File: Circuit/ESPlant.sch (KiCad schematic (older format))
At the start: 13 parts

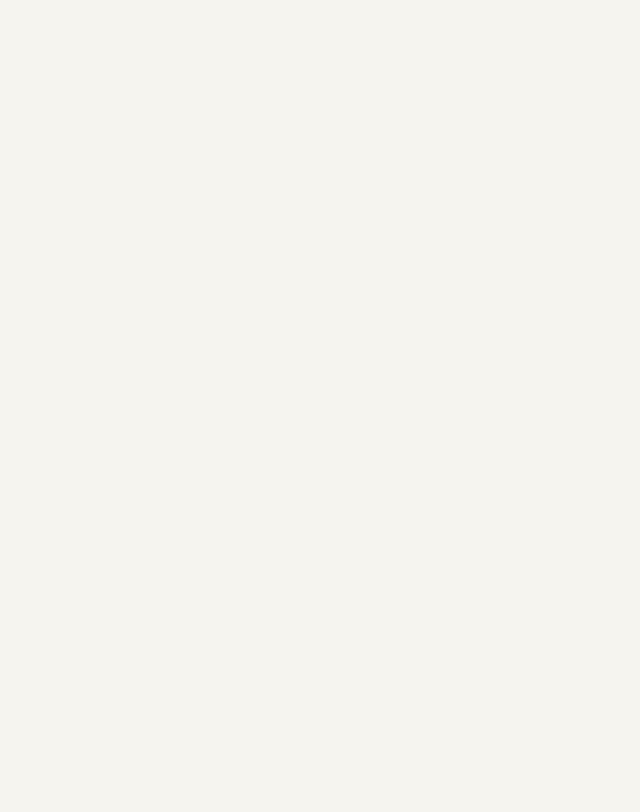
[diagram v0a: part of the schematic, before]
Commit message: Added UFQFPN48 footprint
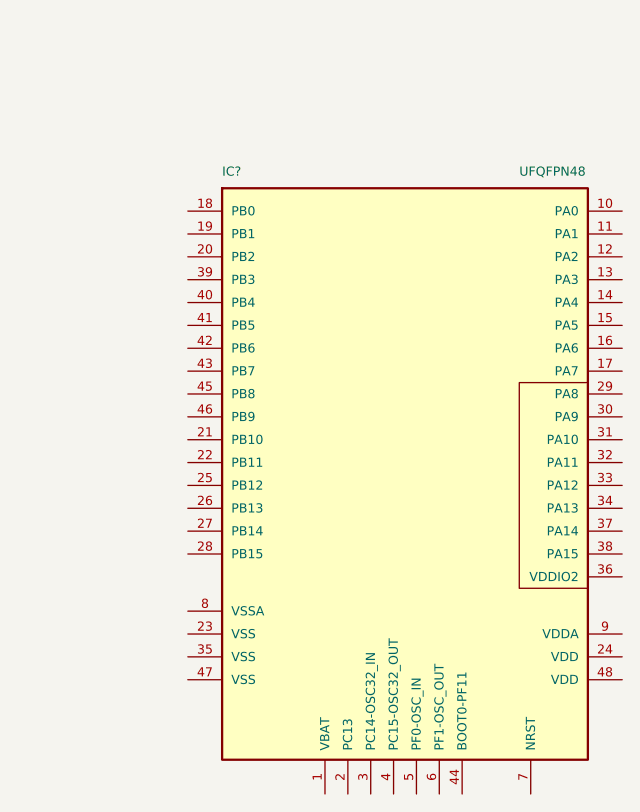
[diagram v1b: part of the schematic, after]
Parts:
- added IC?: UFQFPN48, symbol UFQFPN48
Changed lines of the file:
@@
 LIBS:valves
 LIBS:freetronics_schematic
-LIBS:basic_esp_board-cache
-LIBS:espkit-07-cache
 LIBS:ESPlant
 LIBS:ESPlant-cache
@@
 $EndComp
 NoConn ~ 3900 1700
+$Comp
+L UFQFPN48 IC?
+U 1 1 56379803
+P 5250 4000
+F 0 "IC?" H 4500 5250 40  0000 L BNN
+F 1 "UFQFPN48" H 5800 5250 40  0000 L BNN
+F 2 "" H 5250 4000 30  0000 C CIN
+F 3 "" H 5250 4000 60  0000 C CNN
+	1    5250 4000
+	1    0    0    -1
+$EndComp
 $EndSCHEMATC

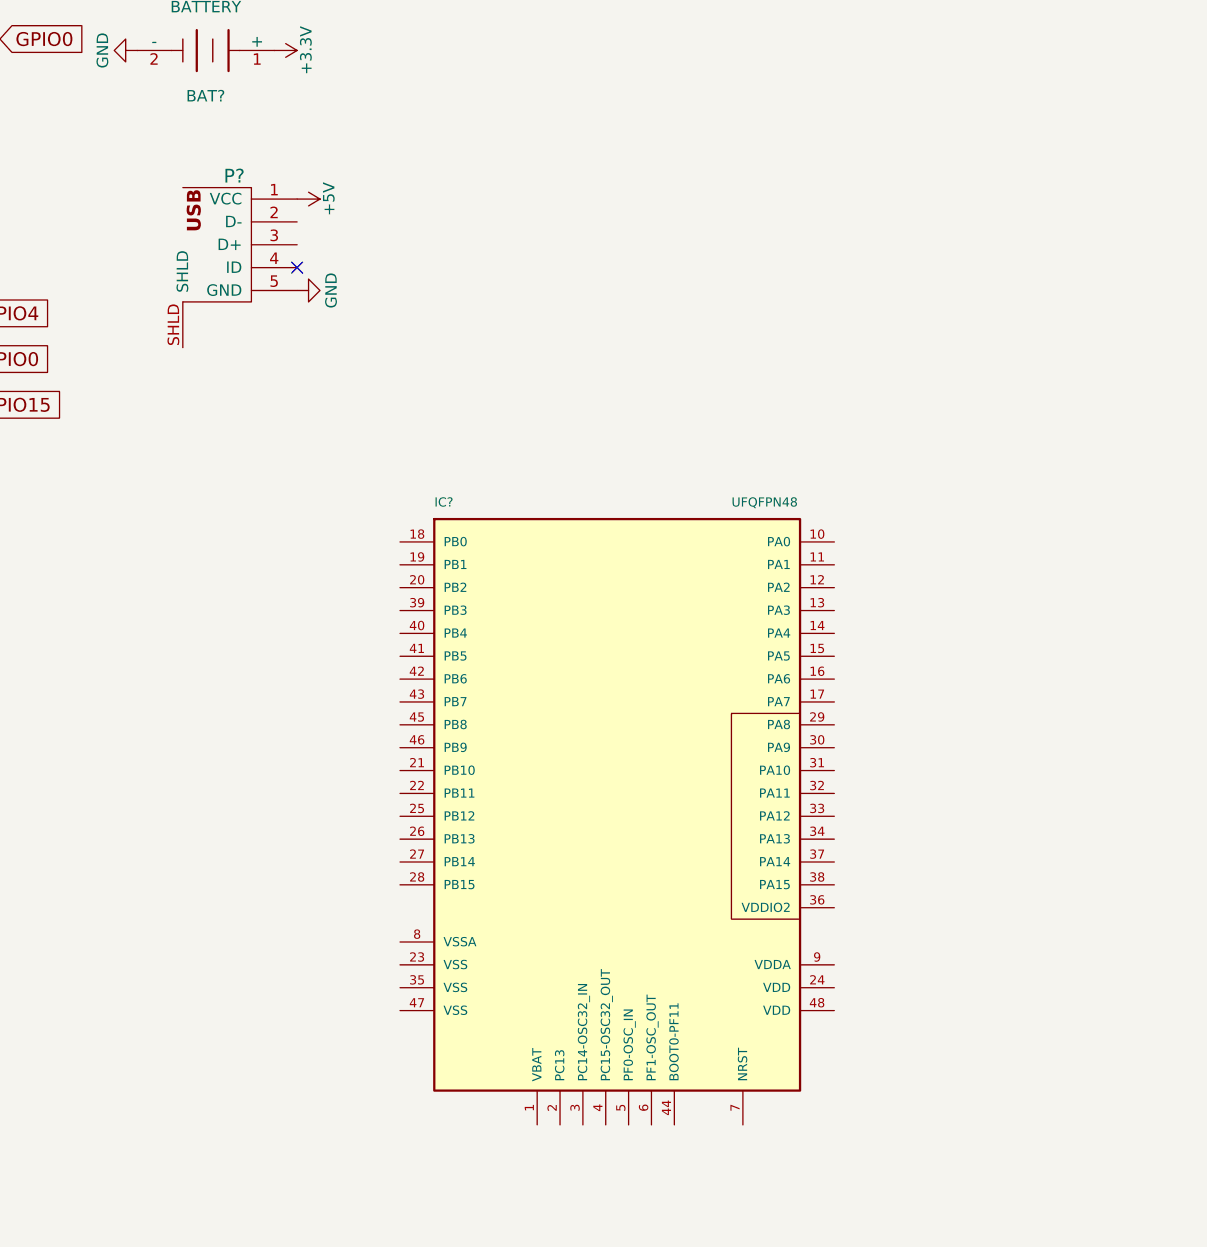
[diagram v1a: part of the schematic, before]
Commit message: Updated UFQFPN48 Footprint
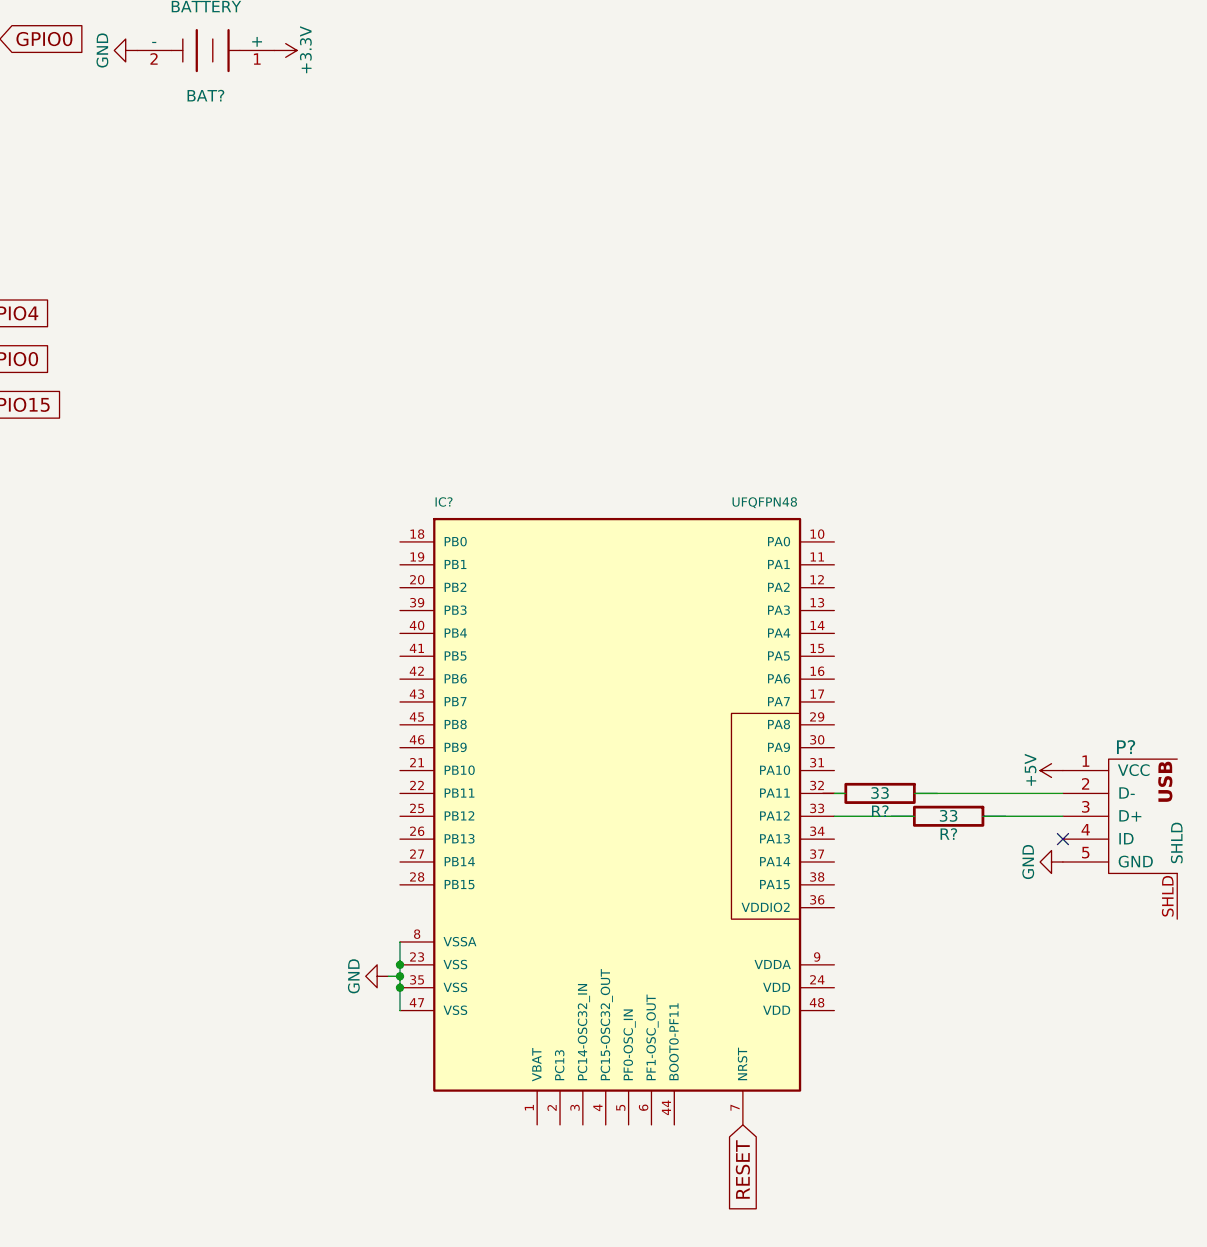
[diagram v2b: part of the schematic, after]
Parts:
- added R? (x2): 33, symbol R
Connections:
- wire segments 11 -> 17
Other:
- moved on the sheet: P?
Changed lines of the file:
@@
 L USB_5PIN_SHELL P?
 U 1 1 56377743
-P 3700 1550
-F 0 "P?" H 3625 1800 60  0000 C CNN
-F 1 "USB_5PIN_SHELL" H 3550 1200 60  0001 L CNN
-F 2 "FT:USB-MICRO_TH_4PEGS" H 3550 1150 31  0001 L CNN
-F 3 "" H 3700 1550 60  0000 C CNN
-	1    3700 1550
-	1    0    0    -1
+P 7450 4050
+F 0 "P?" H 7375 4300 60  0000 C CNN
+F 1 "USB_5PIN_SHELL" H 7300 3700 60  0001 L CNN
+F 2 "FT:USB-MICRO_TH_4PEGS" H 7300 3650 31  0001 L CNN
+F 3 "" H 7450 4050 60  0000 C CNN
+	1    7450 4050
+	-1   0    0    -1
 $EndComp
 $Comp
 L GND #PWR?
 U 1 1 56377AB6
-P 3900 1800
-F 0 "#PWR?" H 3900 1550 50  0001 C CNN
-F 1 "GND" H 3900 1650 50  0000 C CNN
-F 2 "" H 3900 1800 60  0000 C CNN
-F 3 "" H 3900 1800 60  0000 C CNN
-	1    3900 1800
-	0    -1   -1   0
+P 7250 4300
+F 0 "#PWR?" H 7250 4050 50  0001 C CNN
+F 1 "GND" H 7250 4150 50  0000 C CNN
+F 2 "" H 7250 4300 60  0000 C CNN
+F 3 "" H 7250 4300 60  0000 C CNN
+	1    7250 4300
+	0    1    -1   0
 $EndComp
 $Comp
@@
 L +5V #PWR?
 U 1 1 56378962
-P 3900 1400
-F 0 "#PWR?" H 3900 1250 50  0001 C CNN
-F 1 "+5V" H 3900 1540 50  0000 C CNN
-F 2 "" H 3900 1400 60  0000 C CNN
-F 3 "" H 3900 1400 60  0000 C CNN
-	1    3900 1400
-	0    1    1    0
+P 7250 3900
+F 0 "#PWR?" H 7250 3750 50  0001 C CNN
+F 1 "+5V" H 7250 4040 50  0000 C CNN
+F 2 "" H 7250 3900 60  0000 C CNN
+F 3 "" H 7250 3900 60  0000 C CNN
+	1    7250 3900
+	0    -1   1    0
 $EndComp
-NoConn ~ 3900 1700
+NoConn ~ 7250 4200
 $Comp
 L UFQFPN48 IC?
@@
 	1    0    0    -1
 $EndComp
+Text GLabel 5850 5450 3    60   Input ~ 0
+RESET
+$Comp
+L GND #PWR?
+U 1 1 56379DB5
+P 4300 4800
+F 0 "#PWR?" H 4300 4550 50  0001 C CNN
+F 1 "GND" H 4300 4650 50  0000 C CNN
+F 2 "" H 4300 4800 60  0000 C CNN
+F 3 "" H 4300 4800 60  0000 C CNN
+	1    4300 4800
+	0    1    1    0
+$EndComp
+Wire Wire Line
+	4350 4650 4350 4950
+Connection ~ 4350 4750
+Connection ~ 4350 4850
+Wire Wire Line
+	4300 4800 4350 4800
+Connection ~ 4350 4800
+$Comp
+L R R?
+U 1 1 5637A47F
+P 6450 4000
+F 0 "R?" V 6530 4000 50  0000 C CNN
+F 1 "33" V 6450 4000 50  0000 C CNN
+F 2 "" V 6380 4000 30  0000 C CNN
+F 3 "" H 6450 4000 30  0000 C CNN
+	1    6450 4000
+	0    1    1    0
+$EndComp
+$Comp
+L R R?
+U 1 1 5637A511
+P 6750 4100
+F 0 "R?" V 6830 4100 50  0000 C CNN
+F 1 "33" V 6750 4100 50  0000 C CNN
+F 2 "" V 6680 4100 30  0000 C CNN
+F 3 "" H 6750 4100 30  0000 C CNN
+	1    6750 4100
+	0    1    1    0
+$EndComp
+Wire Wire Line
+	7250 4000 6600 4000
+Wire Wire Line
+	6300 4000 6250 4000
+Wire Wire Line
+	6250 4100 6600 4100
+Wire Wire Line
+	6900 4100 7250 4100
 $EndSCHEMATC

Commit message: Updated Lithium power circuit
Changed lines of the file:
@@
 EESchema Schematic File Version 2
+LIBS:freetronics_schematic
 LIBS:power
 LIBS:device
@@
 LIBS:contrib
 LIBS:valves
-LIBS:freetronics_schematic
 LIBS:ESPlant
 LIBS:ESPlant-cache
@@
 $Descr A4 11693 8268
 encoding utf-8
-Sheet 1 1
+Sheet 1 2
 Title ""
 Date ""
@@
 Wire Wire Line
 	6900 4100 7250 4100
+$Sheet
+S 7500 950  2850 1900
+U 563C492E
+F0 "Power" 60
+F1 "Power.sch" 60
+$EndSheet
 $EndSCHEMATC

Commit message: Updated to use esp12e
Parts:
- removed BAT?: BATTERY, symbol BATTERY
- removed P?: ESP-07, symbol ESP-07
- added P1: SOLAR, symbol CONN_01X02
- added U1: ESP-12E, symbol ESP-12E
- gave numbers to parts that had none: 14
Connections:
- net labels added: CSO, GPIO10, GPIO9, MISO, MOSI, SCLK, USB_VCC
- wire segments 17 -> 21
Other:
- moved on the sheet: D2, Q1, R3

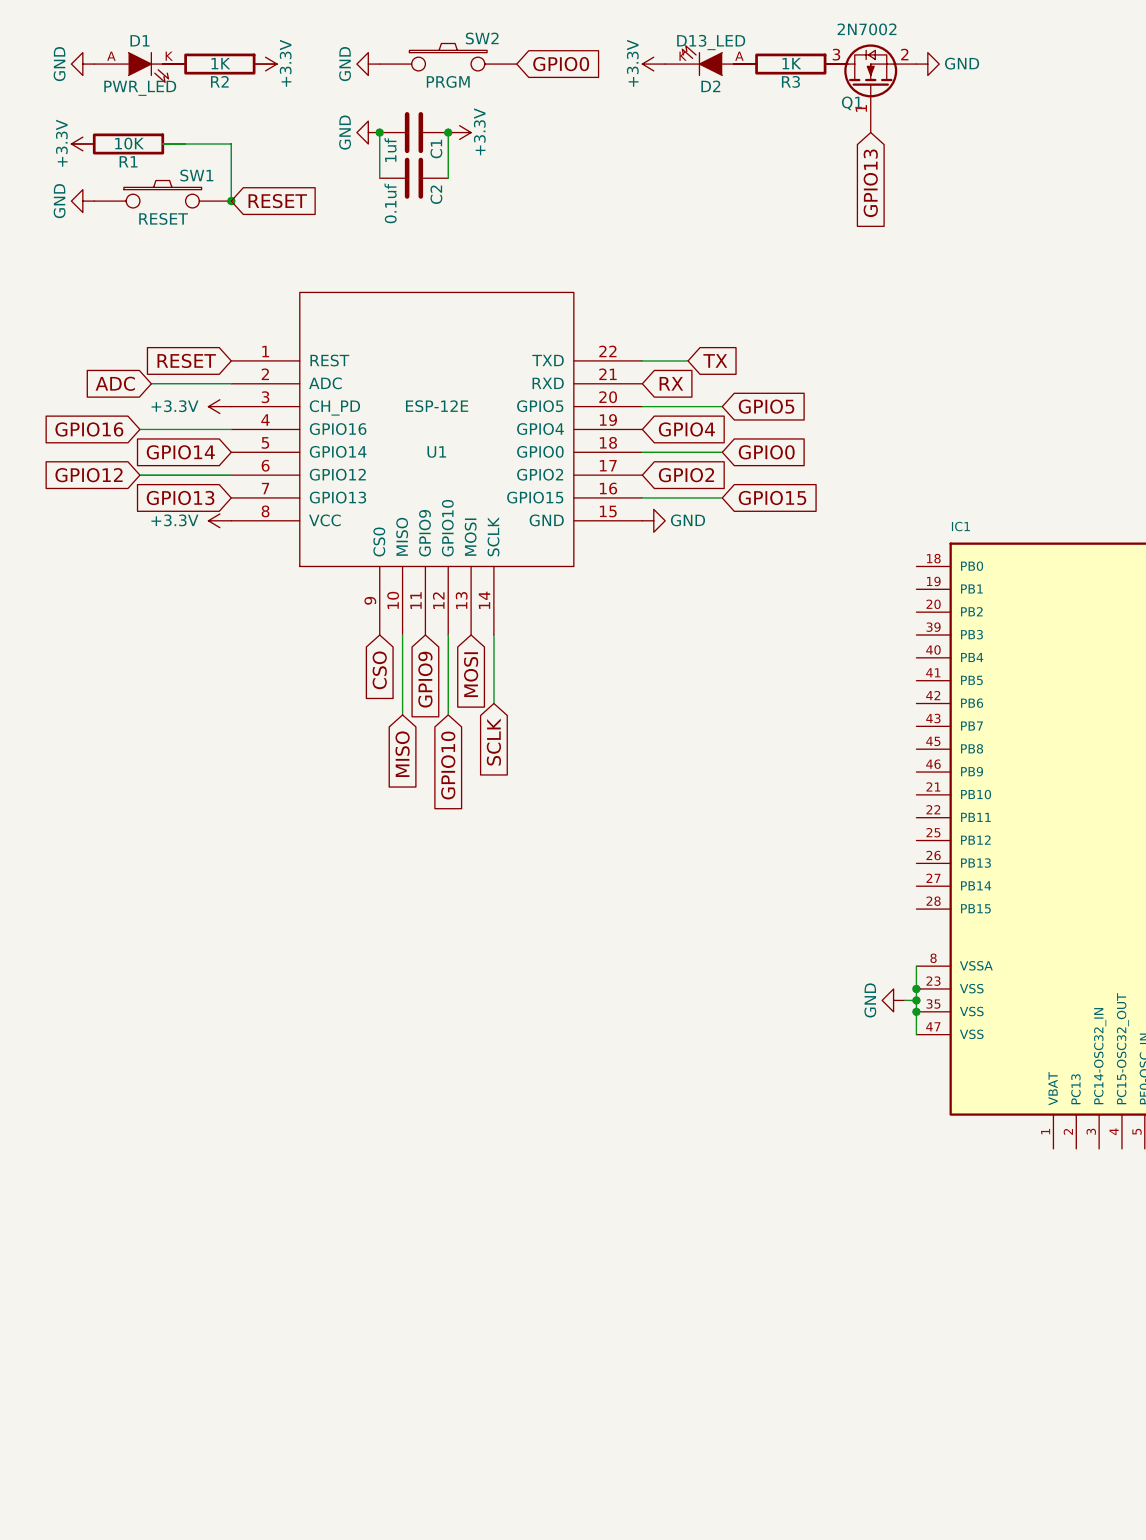
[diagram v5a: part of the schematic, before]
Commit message: Cleaned up main circuit diagram
Added some resistors where there weren't none...
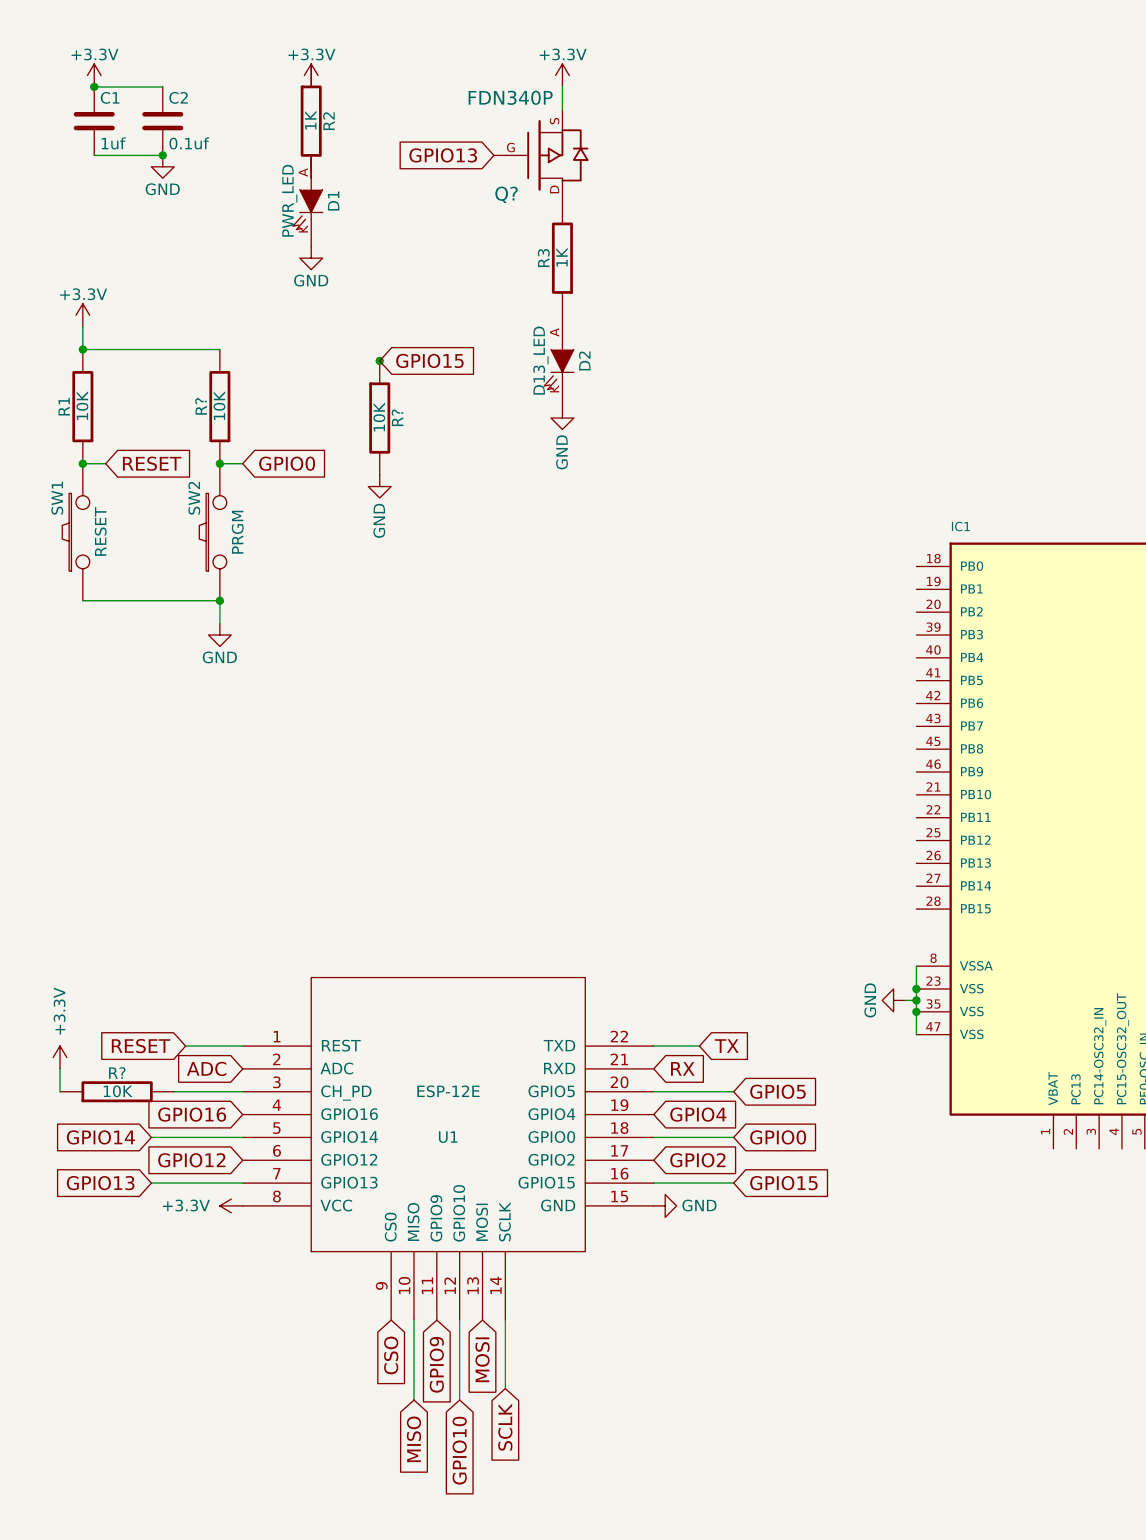
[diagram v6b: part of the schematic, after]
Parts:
- removed Q1: 2N7002, symbol 2N7002
- added Q?: FDN340P, symbol MOSFET_P
- added R? (x3): 10K, symbol R
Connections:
- wire segments 21 -> 31
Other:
- moved on the sheet: C1, C2, D1, D2, R1, R2, R3, SW1, SW2, U1
